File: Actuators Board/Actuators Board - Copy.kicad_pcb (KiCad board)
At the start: 2 copper layers, 93 parts, among them J1 Conn_01x05_Male, J10 Conn_01x02_Male, J3 USB_C_Receptacle_USB2.0, J4 Conn_01x03_Male, J5 Conn_01x06_Male, J9 Conn_01x02_Male, Q1 MMDT2222A, Q2 SI2366DS, U1 ESP32-PICO-D4, U2 TPS54233D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

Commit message: copied files and fixed usb
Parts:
- removed D10: D_Small, Diode_SMD:D_0805_2012Metric
- removed J1: Conn_01x05_Male, Connector_PinHeader_2.54mm:PinHeader_1x05_P2.54mm_Vertical
- removed R13: 10k, Resistor_SMD:R_0603_1608Metric
- removed R_SENS1: 50m, Resistor_SMD:R_0603_1608Metric
- removed TP22: TestPoint, TestPoint:TestPoint_THTPad_1.0x1.0mm_Drill0.5mm
- added C21: 22uF, Capacitor_SMD:C_0603_1608Metric, F.Cu at (185.8, 50.6)
- added C22: 4.7uF, Capacitor_SMD:C_0603_1608Metric, F.Cu at (165.9, 86.2)
- added C23: 4.7uF, Capacitor_SMD:C_0603_1608Metric, F.Cu at (202.8, 38.3)
- added D11: V8PAM10S, iclr:DIO_V3PAN50-M3_I, F.Cu at (68.5, 93.5)
- added D12: V8PAM10S, iclr:DIO_V3PAN50-M3_I, F.Cu at (79.5, 93.4)
- added IC1: BD62120AEFJ-E2, iclr:SOIC127P600X100-9N, F.Cu at (74.0, 96.4)
- added U6: AZ1084-3.3, Package_TO_SOT_SMD:TO-252-3_TabPin2, F.Cu at (191.6, 41.3)
- added U7: LTC4411, Package_TO_SOT_SMD:SOT-23-5, F.Cu at (194.4, 49.1)
- C1, C3: value 0.1uF -> 1uF
- C14: footprint Capacitor_SMD:C_0603_1608Metric -> Capacitor_SMD:C_1210_3225Metric
- C17: value 1uF -> 0.1uF
- C18: value 10uF -> 4.7uF
- C19: value 470uF -> 100uF; footprint Capacitor_SMD:CP_Elec_8x6.7 -> Capacitor_SMD:CP_Elec_5x5.9
- C20: value 100uF -> 10uF
- C7: value 4.7uF -> 10uF; footprint Capacitor_SMD:CP_Elec_3x5.3 -> Capacitor_SMD:C_1210_3225Metric
- D8: value B340 -> MBR260HWTR; footprint Diode_SMD:D_SMC -> Diode_SMD:D_SOD-123
- D9: value D -> V8PAM10S; footprint Diode_SMD:D_0603_1608Metric -> iclr:DIO_V3PAN50-M3_I
- J4: footprint Connector_PinHeader_2.54mm:PinHeader_1x03_P2.54mm_Vertical -> Connector_JST:JST_XH_B3B-XH-AM_1x03_P2.50mm_Vertical
- L1: footprint Inductor_SMD:L_0402_1005Metric_Pad0.77x0.64mm_HandSolder -> Inductor_SMD:L_0603_1608Metric_Pad1.05x0.95mm_HandSolder
- L2: value PE-92111KNL -> ETQP5M; footprint Inductor_SMD:L_12x12mm_H6mm -> iclr:IND_ETQP5M330YFM
- R12: value 1k -> 10k
- R3: value 470 -> 24k
- R4: value 470 -> 3.5k
- R6: value 1k -> 47k
- U5: value MAX14871EUE+ -> LTC4411; footprint iclr:SOP65P637X110-16N -> Package_TO_SOT_SMD:SOT-23-5
- moved Q2 188.2 mm to (258.4, 37.5)
- moved TP24 162.0 mm to (267.6, 64.1)
- moved TP6 157.8 mm to (264.5, 64.1)
- moved TP15 156.8 mm to (267.6, 67.2)
- moved TP10 154.9 mm to (258.4, 67.2)
- moved TP2 154.9 mm to (258.4, 64.1)
- moved TP16 153.7 mm to (264.5, 67.2)
- moved U4 143.5 mm to (244.5, 34.7)
- moved R21 142.3 mm to (258.4, 32.8)
- moved TP11 140.3 mm to (261.5, 64.1)
- moved TP13 138.9 mm to (260.5, 70.2)
- moved TP14 136.4 mm to (263.5, 70.2)
- moved TP12 133.9 mm to (269.4, 61.0)
- moved TP4 133.8 mm to (260.2, 61.0)
- moved TP20 127.1 mm to (251.3, 68.1)
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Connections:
- C10 pad 2: VBUS -> +3V3
- C18 pad 1: +6V -> GND
- C18 pad 2: GND -> +3V3
- C20 pad 1: +6V -> GND
- C20 pad 2: GND -> VBUS
- C7 pad 1: GND -> +24V
- C7 pad 2: Net-(C7-Pad2) -> GND
- C8 pad 2: VBUS -> +3V3
- C9 pad 2: Net-(C7-Pad2) -> +3V3
- Q2 pad 1: /SolEN -> Net-(Q2-Pad1)
- R12 pad 1: +24V -> /SolEN
- R12 pad 2: Net-(R12-Pad2) -> GND
- R21 pad 1: /SolEN -> Net-(Q2-Pad1)
- R21 pad 2: GND -> /SolEN
- R3 pad 1: Net-(R3-Pad1) -> VBUS
- R3 pad 2: GND -> (no net)
- R4 pad 1: Net-(R3-Pad1) -> +24V
- R6 pad 1: Net-(R12-Pad2) -> GND
- R6 pad 2: Net-(R3-Pad1) -> Net-(R3-Pad2)
- TP16 pad 1: /HBridgePWM -> /HBridgeDIR2
- TP24 pad 1: /HBridgeDIR -> /HBridgeDIR1
- U1 pad 15: /HBridgeDIR -> /HBridgeDIR1
- U1 pad 16: /HBridgePWM -> /HBridgeDIR2
- U1 pad 17: unconnected-(U1-Pad17) -> /ServoPWM
- U1 pad 18: /SolEN -> unconnected-(U1-Pad18)
- U1 pad 20: /ServoPWM -> unconnected-(U1-Pad20)
- U1 pad 21: unconnected-(U1-Pad21) -> /SolEN
- U3 pad 6: Net-(C7-Pad2) -> +3V3
- U3 pad 7: VBUS -> +3V3
- U3 pad 8: VBUS -> Net-(R3-Pad2)
- U5 pad 1: /COMM -> (no net)
- U5 pad 2: /Motor+ -> GND
- U5 pad 3: /Motor+ -> GND
- U5 pad 4: +24V -> (no net)
- U5 pad 5: /COMM -> +3V3
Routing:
- net +3V3: track 10.2 -> 55.6 mm, vias 0 -> 4
- net +6V: track 0.00 -> 33.4 mm, vias 0 -> 2
- net /EN: track 0.00 -> 31.0 mm, vias 0 -> 3
- net +24V: track 0.00 -> 18.6 mm
- net VBUS: track 46.5 -> 28.7 mm
- net Net-(C16-Pad2): track 0.00 -> 14.8 mm
- net Net-(C7-Pad2): track 13.1 -> 0.00 mm
- net GND: track 23.8 -> 34.1 mm
- net /BOOT: track 0.00 -> 9.52 mm
- net /DTR: track 0.00 -> 8.69 mm
- net /VSENSE: track 0.00 -> 8.10 mm
- net /RTS: track 0.00 -> 7.27 mm
- net Net-(R17-Pad2): track 2.49 -> 7.49 mm
- net /USB -> UART/Data+: track 25.4 -> 20.9 mm
- net Net-(C1-Pad1): track 0.00 -> 4.39 mm
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
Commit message: Finished usb
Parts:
- moved C18 144.7 mm to (202.8, 36.7)
- moved C20 19.9 mm to (202.3, 43.7)
- moved C21 16.2 mm to (200.0, 42.8), turned to 90 degrees
- moved U7 11.7 mm to (202.9, 41.0)
- moved U6 10.5 mm to (198.3, 49.3), turned to 180 degrees
- moved TP19 1.16 mm to (203.7, 33.5)
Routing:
- net Net-(C21-Pad2): track 0.00 -> 18.6 mm
- net GND: track 34.1 -> 44.0 mm
- net VBUS: track 28.7 -> 38.2 mm, vias 2 -> 3
- net +3V3: track 55.6 -> 59.0 mm
- net /USB -> UART/Data+: track 20.9 -> 20.4 mm

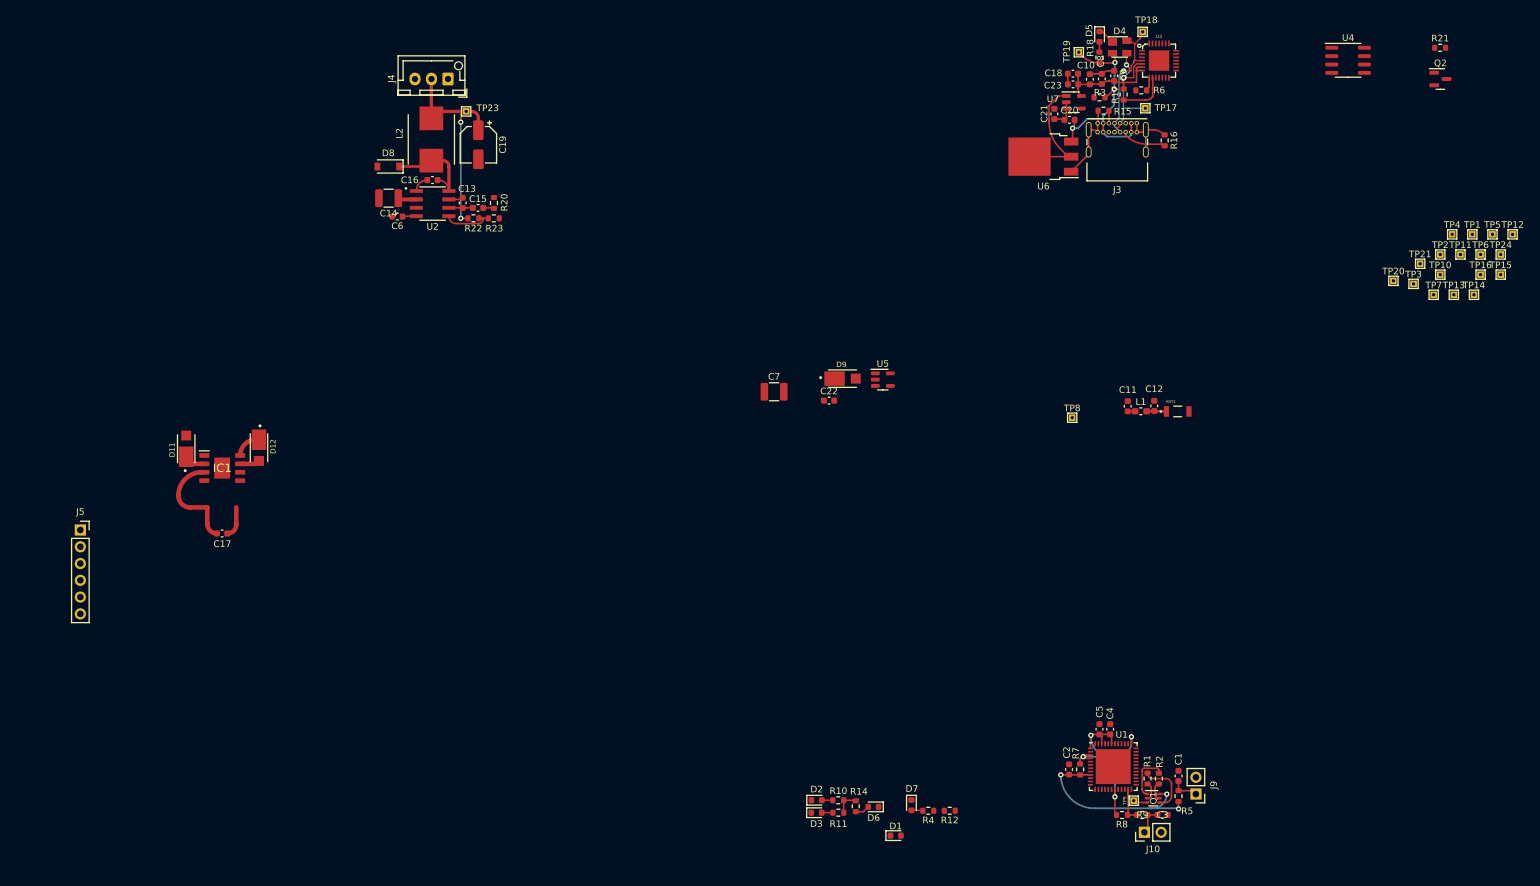
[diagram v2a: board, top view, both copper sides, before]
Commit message: solenoid tracked
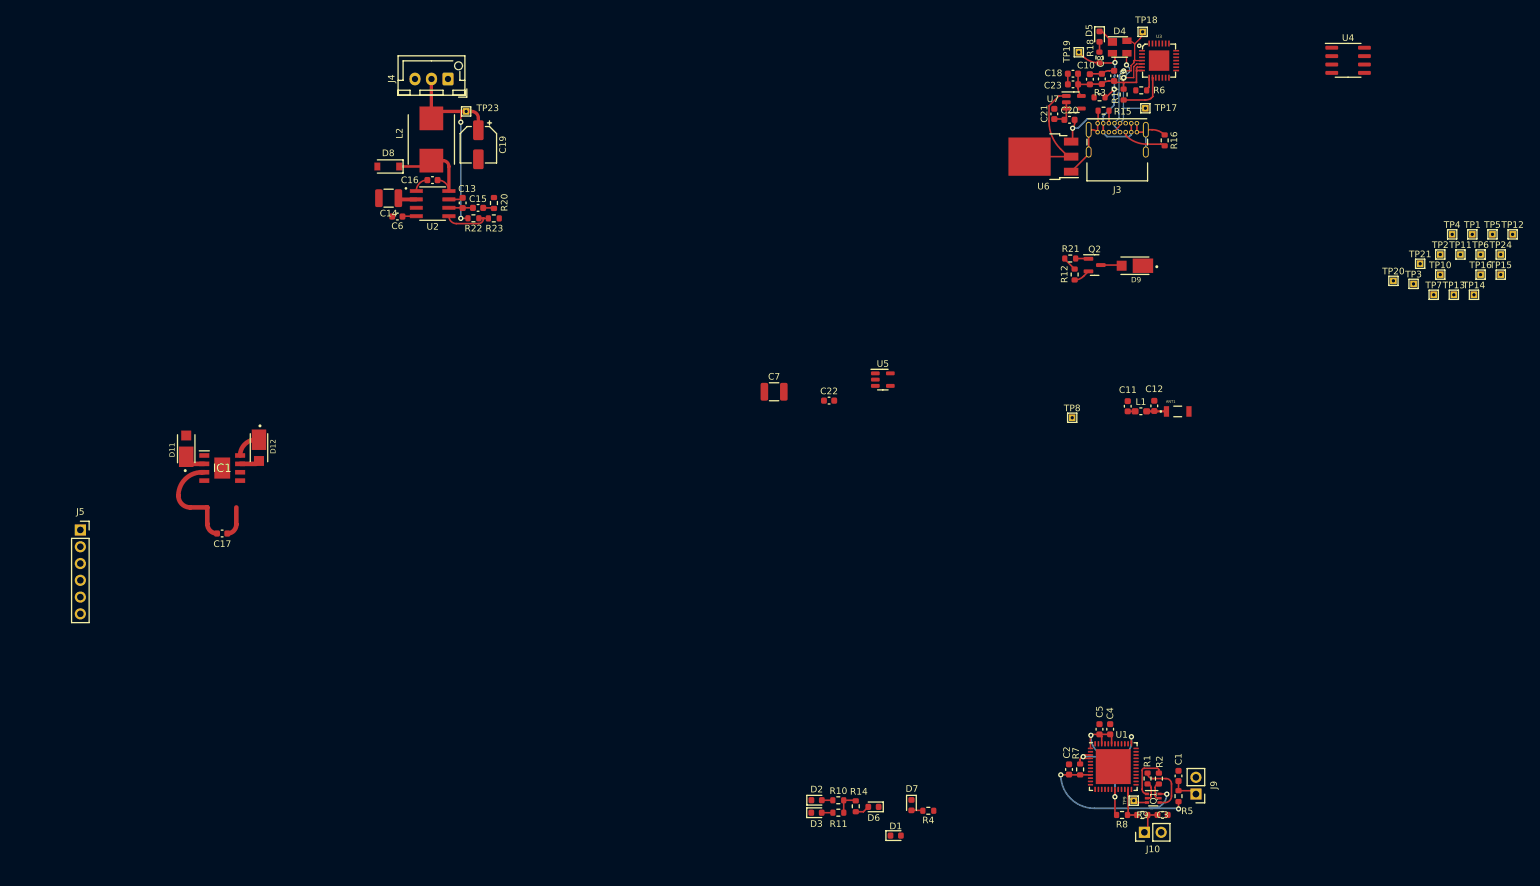
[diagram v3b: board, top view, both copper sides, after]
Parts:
- moved R12 83.4 mm to (203.1, 67.1), turned to -90 degrees
- moved R21 64.5 mm to (202.4, 64.7), turned to 180 degrees
- moved Q2 59.5 mm to (206.1, 65.7)
- moved D9 47.5 mm to (212.2, 65.8), turned to 180 degrees
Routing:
- net /SolGND: track 0.00 -> 3.18 mm
- net GND: track 44.0 -> 46.6 mm
- net /SolEN: track 0.00 -> 2.20 mm
- net Net-(Q2-Pad1): track 0.00 -> 1.95 mm
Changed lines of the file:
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@@
   )
   (footprint "Resistor_SMD:R_0603_1608Metric" (layer "F.Cu")
-    (at 258.42 32.79)
+    (at 202.39 64.71 180)
     (descr "Resistor SMD 0603 (1608 Metric), square (rectangular) end terminal, IPC_7351 nominal, (Body size source: IPC-SM-782 page 72, https://www.pcb-3d.com/wordpress/wp-content/uploads/ipc-sm-782a_amendment_1_and_2.pdf), generated with kicad-footprint-generator")
     (tags "resistor")
@@
     (property "Sheetname" "")
     (attr smd)
-    (fp_text reference "R21" (at 0 -1.43) (layer "F.SilkS")
+    (fp_text reference "R21" (at -0.06 1.46) (layer "F.SilkS")
       (effects (font (size 1 1) (thickness 0.15)))
     )
@@
     (fp_line (start 0.8 0.4125) (end -0.8 0.4125) (layer "F.Fab") (width 0.1))
     (fp_line (start 0.8 -0.4125) (end 0.8 0.4125) (layer "F.Fab") (width 0.1))
-    (pad "1" smd roundrect (at -0.825 0) (size 0.8 0.95) (layers "F.Cu" "F.Paste" "F.Mask") (roundrect_rratio 0.25)
+    (pad "1" smd roundrect (at -0.825 0 180) (size 0.8 0.95) (layers "F.Cu" "F.Paste" "F.Mask") (roundrect_rratio 0.25)
       (net 35 "Net-(Q2-Pad1)") (pintype "passive"))
-    (pad "2" smd roundrect (at 0.825 0) (size 0.8 0.95) (layers "F.Cu" "F.Paste" "F.Mask") (roundrect_rratio 0.25)
+    (pad "2" smd roundrect (at 0.825 0 180) (size 0.8 0.95) (layers "F.Cu" "F.Paste" "F.Mask") (roundrect_rratio 0.25)
       (net 31 "/SolEN") (pintype "passive"))
     (model "${KICAD6_3DMODEL_DIR}/Resistor_SMD.3dshapes/R_0603_1608Metric.wrl"
@@
   )
   (footprint "Resistor_SMD:R_0603_1608Metric" (layer "F.Cu")
-    (at 184.14 148.35 180)
+    (at 203.06 67.13 -90)
     (descr "Resistor SMD 0603 (1608 Metric), square (rectangular) end terminal, IPC_7351 nominal, (Body size source: IPC-SM-782 page 72, https://www.pcb-3d.com/wordpress/wp-content/uploads/ipc-sm-782a_amendment_1_and_2.pdf), generated with kicad-footprint-generator")
     (tags "resistor")
@@
     (property "Sheetname" "")
     (attr smd)
-    (fp_text reference "R12" (at 0 -1.43) (layer "F.SilkS")
-      (effects (font (size 1 1) (thickness 0.15)))
-    )
-    (fp_text value "10k" (at 0 1.43) (layer "F.Fab")
-      (effects (font (size 1 1) (thickness 0.15)))
-    )
-    (fp_text user "${REFERENCE}" (at 0 0) (layer "F.Fab")
+    (fp_text reference "R12" (at -0.05 1.55 -270) (layer "F.SilkS")
+      (effects (font (size 1 1) (thickness 0.15)))
+    )
+    (fp_text value "10k" (at 0 1.43 -270) (layer "F.Fab")
+      (effects (font (size 1 1) (thickness 0.15)))
+    )
+    (fp_text user "${REFERENCE}" (at 0 0 -270) (layer "F.Fab")
       (effects (font (size 0.4 0.4) (thickness 0.06)))
     )
@@
     (fp_line (start 0.8 0.4125) (end -0.8 0.4125) (layer "F.Fab") (width 0.1))
     (fp_line (start 0.8 -0.4125) (end 0.8 0.4125) (layer "F.Fab") (width 0.1))
-    (pad "1" smd roundrect locked (at -0.825 0 180) (size 0.8 0.95) (layers "F.Cu" "F.Paste" "F.Mask") (roundrect_rratio 0.25)
+    (pad "1" smd roundrect locked (at -0.825 0 270) (size 0.8 0.95) (layers "F.Cu" "F.Paste" "F.Mask") (roundrect_rratio 0.25)
       (net 31 "/SolEN") (pintype "passive"))
-    (pad "2" smd roundrect locked (at 0.825 0 180) (size 0.8 0.95) (layers "F.Cu" "F.Paste" "F.Mask") (roundrect_rratio 0.25)
+    (pad "2" smd roundrect locked (at 0.825 0 270) (size 0.8 0.95) (layers "F.Cu" "F.Paste" "F.Mask") (roundrect_rratio 0.25)
       (net 2 "GND") (pintype "passive"))
     (model "${KICAD6_3DMODEL_DIR}/Resistor_SMD.3dshapes/R_0603_1608Metric.wrl"
@@
   )
   (footprint "iclr:DIO_V3PAN50-M3_I" (layer "F.Cu")
-    (at 167.902 82.9)
+    (at 212.19 65.8 180)
     (property "MANUFACTURER" "Vishay")
     (property "PARTREV" "20-Oct-16")
@@
     (fp_line (start -2.125 1.3) (end -2.125 -1.3) (layer "F.Fab") (width 0.127))
     (fp_line (start -2.125 -1.3) (end 2.125 -1.3) (layer "F.Fab") (width 0.127))
-    (pad "A" smd rect locked (at 2.01 0) (size 1.5 1.52) (layers "F.Cu" "F.Paste" "F.Mask")
+    (pad "A" smd rect locked (at 2.01 0 180) (size 1.5 1.52) (layers "F.Cu" "F.Paste" "F.Mask")
       (net 32 "/SolGND") (pintype "passive"))
-    (pad "C" smd rect locked (at -1.21 0) (size 3.1 2.2) (layers "F.Cu" "F.Paste" "F.Mask")
+    (pad "C" smd rect locked (at -1.21 0 180) (size 3.1 2.2) (layers "F.Cu" "F.Paste" "F.Mask")
       (net 11 "+24V") (pintype "passive"))
   )
@@
   )
   (footprint "Package_TO_SOT_SMD:SOT-23" (layer "F.Cu")
-    (at 258.45 37.52)
+    (at 206.09 65.7)
     (descr "SOT, 3 Pin (https://www.jedec.org/system/files/docs/to-236h.pdf variant AB), generated with kicad-footprint-generator ipc_gullwing_generator.py")
     (tags "SOT TO_SOT_SMD")
@@
   (segment (start 205.19 45.2) (end 205.646741 45.2) (width 0.25) (layer "F.Cu") (net 2))
   (segment (start 207.18 36.735) (end 205.42 36.735) (width 0.25) (layer "F.Cu") (net 2))
+  (segment (start 204.404346 67.398153) (end 205.1525 66.65) (width 0.25) (layer "F.Cu") (net 2))
   (segment (start 206.54 44.22) (end 206.54 45.57) (width 0.25) (layer "F.Cu") (net 2))
   (segment (start 206.615 42.32) (end 206.615 44.145) (width 0.25) (layer "F.Cu") (net 2))
@@
   (arc (start 110.13 55.755) (mid 110.299706 55.684706) (end 110.37 55.515) (width 0.25) (layer "F.Cu") (net 2))
   (arc (start 204.963726 49.126274) (mid 205.131193 48.875642) (end 205.19 48.58) (width 0.25) (layer "F.Cu") (net 2))
+  (arc (start 203.06 67.955) (mid 203.787555 67.81028) (end 204.404346 67.398153) (width 0.25) (layer "F.Cu") (net 2))
   (arc (start 79.089002 95.809998) (mid 79.397301 95.682297) (end 79.525002 95.373998) (width 0.25) (layer "F.Cu") (net 2))
   (arc (start 214.787772 45.2) (mid 215.819956 45.405314) (end 216.695 45.99) (width 0.25) (layer "F.Cu") (net 2))
@@
   (arc (start 217.729251 146.125103) (mid 217.44371 146.814459) (end 216.754354 147.1) (width 0.25) (layer "F.Cu") (net 30))
   (arc (start 216.909145 143.475) (mid 217.489048 143.715203) (end 217.729251 144.295106) (width 0.25) (layer "F.Cu") (net 30))
+  (segment (start 201.635711 64.88071) (end 203.06 66.305) (width 0.25) (layer "F.Cu") (net 31))
+  (arc (start 201.565 64.71) (mid 201.583377 64.802388) (end 201.635711 64.88071) (width 0.25) (layer "F.Cu") (net 31))
+  (segment (start 207.0275 65.7) (end 209.938579 65.7) (width 0.25) (layer "F.Cu") (net 32))
+  (arc (start 209.938579 65.7) (mid 210.069235 65.725989) (end 210.18 65.8) (width 0.25) (layer "F.Cu") (net 32))
   (segment (start 202.53 49.23) (end 202.53 49.28) (width 0.25) (layer "F.Cu") (net 33))
   (segment (start 202.5 49.28) (end 202.53 49.28) (width 0.25) (layer "F.Cu") (net 33))
@@
   (segment (start 178.34 148.2875) (end 180.0075 148.2875) (width 0.25) (layer "F.Cu") (net 34))
   (segment (start 180.0075 148.2875) (end 180.07 148.35) (width 0.25) (layer "F.Cu") (net 34))
+  (segment (start 203.215 64.71) (end 205.055932 64.71) (width 0.25) (layer "F.Cu") (net 35))
+  (arc (start 205.055932 64.71) (mid 205.108194 64.720396) (end 205.1525 64.75) (width 0.25) (layer "F.Cu") (net 35))
   (segment (start 166.435 146.76) (end 164.7775 146.76) (width 0.25) (layer "F.Cu") (net 36))
   (segment (start 164.7775 146.76) (end 164.7675 146.75) (width 0.25) (layer "F.Cu") (net 36))
